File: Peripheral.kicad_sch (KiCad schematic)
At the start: 18 parts, among them J10 Conn_01x03, J11 Conn_01x03, J12 Conn_01x03, J2 Conn_01x04, J3 Conn_01x06, J4 Conn_01x06, J5 Conn_01x06, J6 Conn_01x07, J9 Conn_01x03

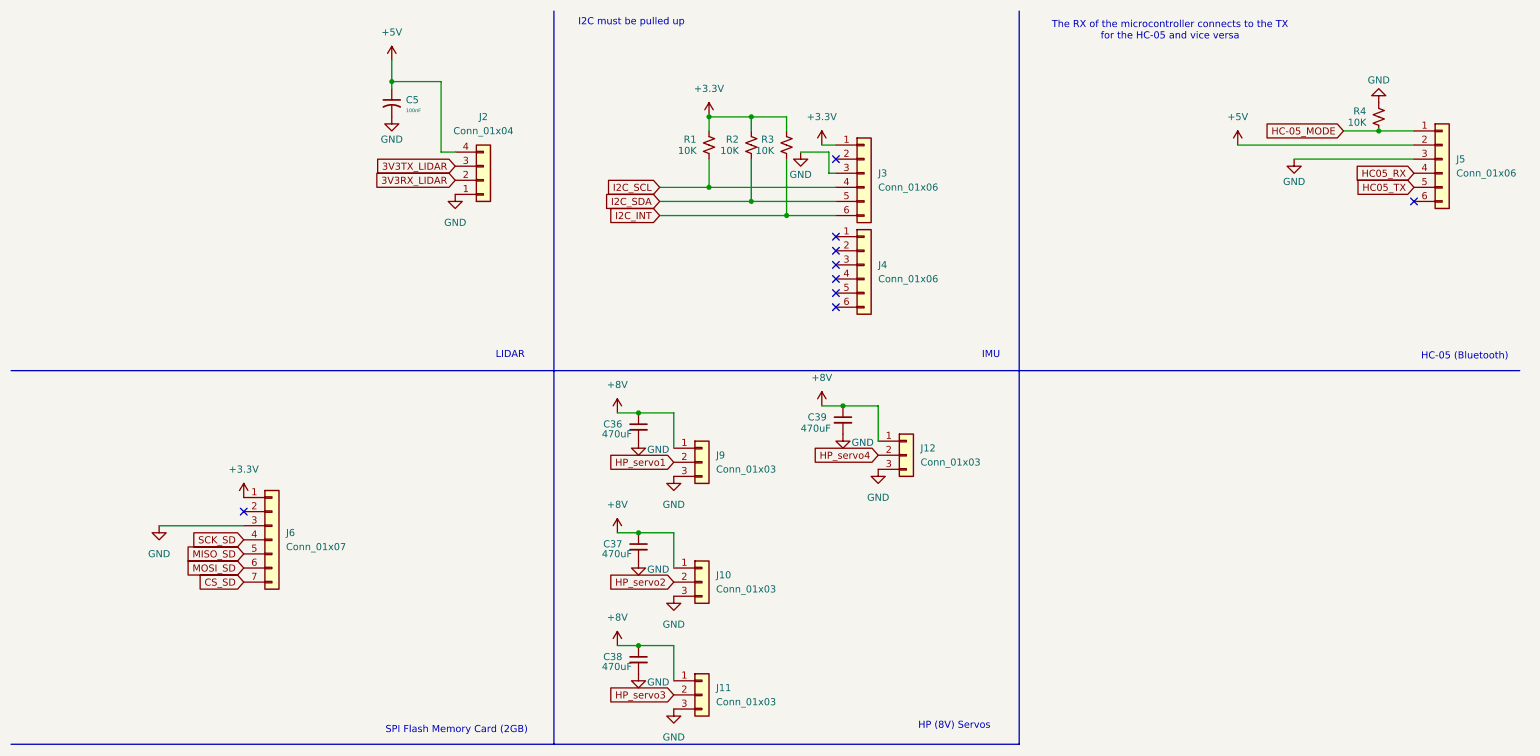
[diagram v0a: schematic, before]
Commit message: General Layout Complete
Completed general layout, beginning to add debugging components such as test points and
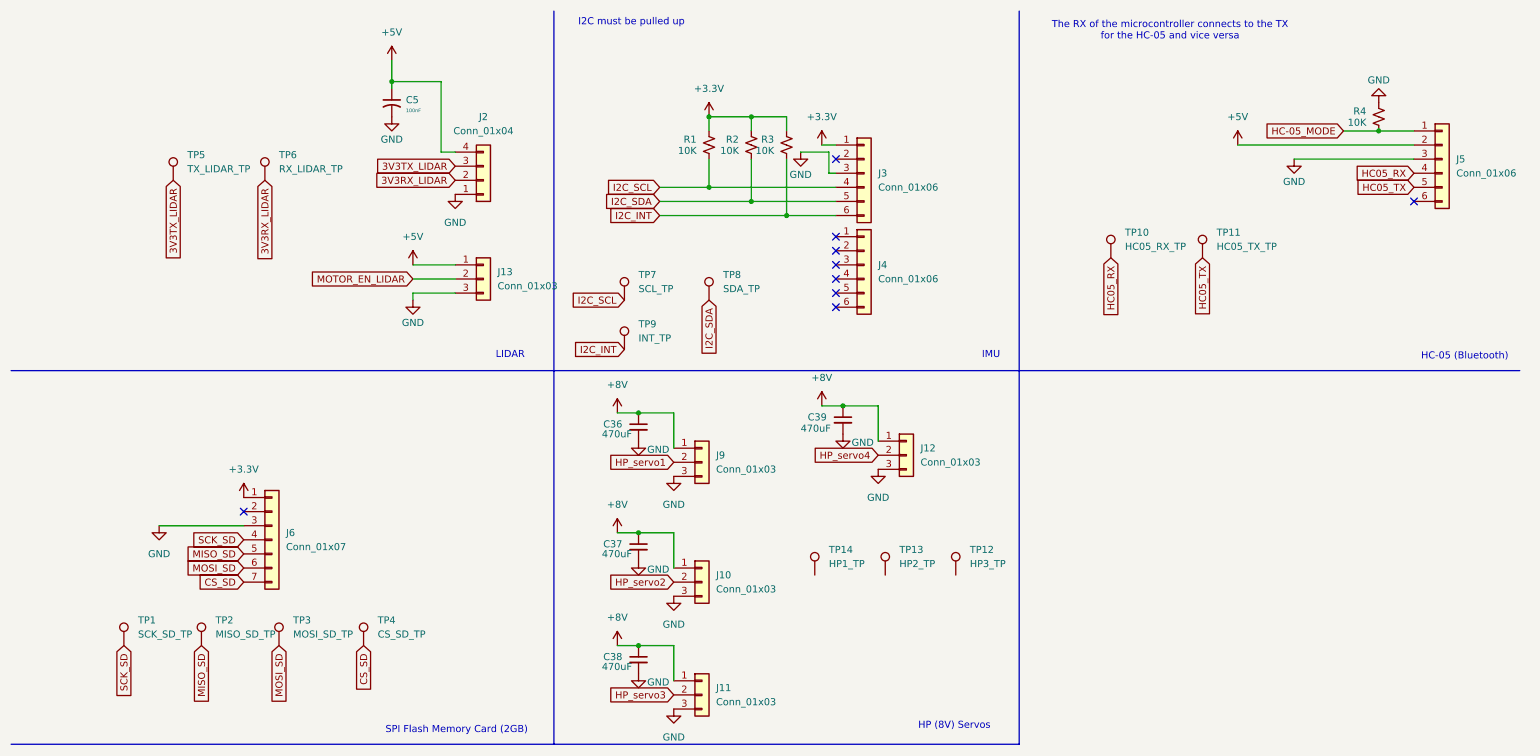
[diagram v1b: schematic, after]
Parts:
- added J13: Conn_01x03, Connector_PinHeader_2.54mm:PinHeader_1x03_P2.54mm_Vertical, symbol Connector_Generic:Conn_01x03
- added TP1: SCK_SD_TP, symbol Connector:TestPoint
- added TP10: HC05_RX_TP, symbol Connector:TestPoint
- added TP11: HC05_TX_TP, symbol Connector:TestPoint
- added TP12: HP3_TP, symbol Connector:TestPoint
- added TP13: HP2_TP, symbol Connector:TestPoint
- added TP14: HP1_TP, symbol Connector:TestPoint
- added TP2: MISO_SD_TP, symbol Connector:TestPoint
- added TP3: MOSI_SD_TP, symbol Connector:TestPoint
- added TP4: CS_SD_TP, symbol Connector:TestPoint
- added TP5: TX_LIDAR_TP, symbol Connector:TestPoint
- added TP6: RX_LIDAR_TP, symbol Connector:TestPoint
- added TP7: SCL_TP, symbol Connector:TestPoint
- added TP8: SDA_TP, symbol Connector:TestPoint
- added TP9: INT_TP, symbol Connector:TestPoint
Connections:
- net +5V: now also J13.1 (Pin_1)
- net 3V3RX_LIDAR: now also TP6.1
- net 3V3TX_LIDAR: now also TP5.1
- net CS_SD: now also TP4.1
- net GND: now also J13.3 (Pin_3)
- net HC05_RX: now also TP10.1
- net HC05_TX: now also TP11.1
- net I2C_INT: now also TP9.1
- net I2C_SCL: now also TP7.1
- net I2C_SDA: now also TP8.1
- net MISO_SD: now also TP2.1
- net MOSI_SD: now also TP3.1
- net SCK_SD: now also TP1.1
- new net MOTOR_EN_LIDAR: J13.2 (Pin_2)

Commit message: update
more work on testpoints
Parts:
- added TP15: HP4_TP, symbol Connector:TestPoint
- added TP16: GND_2, symbol Connector:TestPoint
- added TP17: GND_3, symbol Connector:TestPoint
- added TP18: GND_4, symbol Connector:TestPoint
- added TP19: GND_5, symbol Connector:TestPoint
- added TP20: GND_1, symbol Connector:TestPoint
- added TP21: GND_6, symbol Connector:TestPoint
- added TP22: GND_7, symbol Connector:TestPoint
- added TP23: GND_8, symbol Connector:TestPoint
- added TP24: GND_9, symbol Connector:TestPoint
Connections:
- net GND: now also TP16.1, TP17.1, TP18.1, TP19.1, TP20.1, TP21.1, TP22.1, TP23.1, TP24.1
- net HP_servo1: now also TP14.1
- net HP_servo2: now also TP13.1
- net HP_servo3: now also TP12.1
- net HP_servo4: now also TP15.1
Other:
- note added: "Test points for each motor"
- note added: "Test points for each peripheral"
- moved on the sheet: TP12, TP13

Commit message: testpoints on board
Organized testpoints on board. Still need to fix bus for general purpose GPIO and route traces for LEDs.
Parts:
- TP1, TP10, TP11, TP12, TP13, TP14, TP15, TP16, TP17, TP18, TP19, TP2, TP20, TP21, TP22, TP23, TP24, TP3, TP4, TP5, TP6, TP7, TP8, TP9: footprint (none) -> TestPoint:TestPoint_Keystone_5019_Miniature
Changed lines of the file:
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@@
 			)
 		)
-		(property "Footprint" ""
+		(property "Footprint" "TestPoint:TestPoint_Keystone_5019_Miniature"
 			(at 232.41 57.15 0)
 			(hide yes)
@@
 			)
 		)
-		(property "Footprint" ""
+		(property "Footprint" "TestPoint:TestPoint_Keystone_5019_Miniature"
 			(at 280.67 97.79 0)
 			(hide yes)
@@
 			)
 		)
-		(property "Footprint" ""
+		(property "Footprint" "TestPoint:TestPoint_Keystone_5019_Miniature"
 			(at 215.9 57.15 0)
 			(hide yes)
@@
 			)
 		)
-		(property "Footprint" ""
+		(property "Footprint" "TestPoint:TestPoint_Keystone_5019_Miniature"
 			(at 143.51 64.77 0)
 			(hide yes)
@@
 			)
 		)
-		(property "Footprint" ""
+		(property "Footprint" "TestPoint:TestPoint_Keystone_5019_Miniature"
 			(at 166.37 121.92 0)
 			(hide yes)
@@
 			)
 		)
-		(property "Footprint" ""
+		(property "Footprint" "TestPoint:TestPoint_Keystone_5019_Miniature"
 			(at 177.8 114.3 0)
 			(hide yes)
@@
 			)
 		)
-		(property "Footprint" ""
+		(property "Footprint" "TestPoint:TestPoint_Keystone_5019_Miniature"
 			(at 81.28 127 0)
 			(hide yes)
@@
 			)
 		)
-		(property "Footprint" ""
+		(property "Footprint" "TestPoint:TestPoint_Keystone_5019_Miniature"
 			(at 63.5 43.18 0)
 			(hide yes)
@@
 			)
 		)
-		(property "Footprint" ""
+		(property "Footprint" "TestPoint:TestPoint_Keystone_5019_Miniature"
 			(at 52.07 127 0)
 			(hide yes)
@@
 			)
 		)
-		(property "Footprint" ""
+		(property "Footprint" "TestPoint:TestPoint_Keystone_5019_Miniature"
 			(at 266.7 97.79 0)
 			(hide yes)
@@
 			)
 		)
-		(property "Footprint" ""
+		(property "Footprint" "TestPoint:TestPoint_Keystone_5019_Miniature"
 			(at 162.56 114.3 0)
 			(hide yes)
@@
 			)
 		)
-		(property "Footprint" ""
+		(property "Footprint" "TestPoint:TestPoint_Keystone_5019_Miniature"
 			(at 267.97 120.65 0)
 			(hide yes)
@@
 			)
 		)
-		(property "Footprint" ""
+		(property "Footprint" "TestPoint:TestPoint_Keystone_5019_Miniature"
 			(at 128.27 73.66 0)
 			(hide yes)
@@
 			)
 		)
-		(property "Footprint" ""
+		(property "Footprint" "TestPoint:TestPoint_Keystone_5019_Miniature"
 			(at 238.76 120.65 0)
 			(hide yes)
@@
 			)
 		)
-		(property "Footprint" ""
+		(property "Footprint" "TestPoint:TestPoint_Keystone_5019_Miniature"
 			(at 224.79 97.79 0)
 			(hide yes)
@@
 			)
 		)
-		(property "Footprint" ""
+		(property "Footprint" "TestPoint:TestPoint_Keystone_5019_Miniature"
 			(at 224.79 120.65 0)
 			(hide yes)
@@
 			)
 		)
-		(property "Footprint" ""
+		(property "Footprint" "TestPoint:TestPoint_Keystone_5019_Miniature"
 			(at 38.1 127 0)
 			(hide yes)
@@
 			)
 		)
-		(property "Footprint" ""
+		(property "Footprint" "TestPoint:TestPoint_Keystone_5019_Miniature"
 			(at 189.23 114.3 0)
 			(hide yes)
@@
 			)
 		)
-		(property "Footprint" ""
+		(property "Footprint" "TestPoint:TestPoint_Keystone_5019_Miniature"
 			(at 254 97.79 0)
 			(hide yes)
@@
 			)
 		)
-		(property "Footprint" ""
+		(property "Footprint" "TestPoint:TestPoint_Keystone_5019_Miniature"
 			(at 66.04 127 0)
 			(hide yes)
@@
 			)
 		)
-		(property "Footprint" ""
+		(property "Footprint" "TestPoint:TestPoint_Keystone_5019_Miniature"
 			(at 128.27 64.77 0)
 			(hide yes)
@@
 			)
 		)
-		(property "Footprint" ""
+		(property "Footprint" "TestPoint:TestPoint_Keystone_5019_Miniature"
 			(at 240.03 97.79 0)
 			(hide yes)
@@
 			)
 		)
-		(property "Footprint" ""
+		(property "Footprint" "TestPoint:TestPoint_Keystone_5019_Miniature"
 			(at 46.99 43.18 0)
 			(hide yes)
@@
 			)
 		)
-		(property "Footprint" ""
+		(property "Footprint" "TestPoint:TestPoint_Keystone_5019_Miniature"
 			(at 254 120.65 0)
 			(hide yes)

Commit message: almost completed board
need to clean up silkscreen, run thru checklist and verify, review datasheets
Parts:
- added R25, R26, R27, R28, R29, R30, R31, R32: 22, Resistor_SMD:R_0805_2012Metric_Pad1.20x1.40mm_HandSolder, symbol Device:R_Small_US
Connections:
- net 3V3RX_LIDAR: now also R26.1, R26.2
- net 3V3TX_LIDAR: now also R25.1, R25.2
- net CS_SD: now also R29.1, R29.2
- net HC05_RX: now also R27.1, R27.2
- net HC05_TX: now also R28.1, R28.2
- net MISO_SD: now also R31.1, R31.2
- net MOSI_SD: now also R30.1, R30.2
- net SCK_SD: now also R32.1, R32.2
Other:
- moved on the sheet: TP5, TP6

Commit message: completed v1 board with outputs
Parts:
- added TP25: state hc05, TestPoint:TestPoint_Keystone_5019_Miniature, symbol Connector:TestPoint
- R1, R2, R3: value 10K -> 4.7K
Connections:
- net at J5.6 (Pin_6): now also TP25.1
- no-connect marks 9 -> 8
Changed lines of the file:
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@@
 		(at 54.61 102.87)
 	)
-	(no_connect
-		(at 265.43 46.99)
-	)
 	(wire
 		(pts
@@
 	(wire
 		(pts
+			(xy 265.43 55.88) (xy 250.19 55.88)
+		)
+		(stroke
+			(width 0)
+			(type default)
+		)
+	)
+	(wire
+		(pts
 			(xy 248.92 101.6) (xy 248.92 105.41)
 		)
@@
 	(wire
 		(pts
+			(xy 265.43 46.99) (xy 265.43 55.88)
+		)
+		(stroke
+			(width 0)
+			(type default)
+		)
+	)
+	(wire
+		(pts
 			(xy 219.71 120.65) (xy 219.71 124.46)
 		)
@@
 			)
 		)
-		(property "Value" "10K"
+		(property "Value" "4.7K"
 			(at 140.462 37.846 0)
 			(show_name no)
@@
 			)
 		)
-		(property "Value" "10K"
+		(property "Value" "4.7K"
 			(at 132.842 37.846 0)
 			(show_name no)
@@
 	)
 	(symbol
+		(lib_id "Connector:TestPoint")
+		(at 250.19 55.88 0)
+		(unit 1)
+		(body_style 1)
+		(exclude_from_sim no)
+		(in_bom yes)
+		(on_board yes)
+		(in_pos_files yes)
+		(dnp no)
+		(fields_autoplaced yes)
+		(property "Reference" "TP25"
+			(at 252.73 51.3079 0)
+			(show_name no)
+			(do_not_autoplace no)
+			(effects
+				(font
+					(size 1.27 1.27)
+				)
+				(justify left)
+			)
+		)
+		(property "Value" "state hc05"
+			(at 252.73 53.8479 0)
+			(show_name no)
+			(do_not_autoplace no)
+			(effects
+				(font
+					(size 1.27 1.27)
+				)
+				(justify left)
+			)
+		)
+		(property "Footprint" "TestPoint:TestPoint_Keystone_5019_Miniature"
+			(at 255.27 55.88 0)
+			(hide yes)
+			(show_name no)
+			(do_not_autoplace no)
+			(effects
+				(font
+					(size 1.27 1.27)
+				)
+			)
+		)
+		(property "Datasheet" ""
+			(at 255.27 55.88 0)
+			(hide yes)
+			(show_name no)
+			(do_not_autoplace no)
+			(effects
+				(font
+					(size 1.27 1.27)
+				)
+			)
+		)
+		(property "Description" "test point"
+			(at 250.19 55.88 0)
+			(hide yes)
+			(show_name no)
+			(do_not_autoplace no)
+			(effects
+				(font
+					(size 1.27 1.27)
+				)
+			)
+		)
+		(pin "1"
+		)
+		(instances
+			(project "Bellbot"
+				(path "/e8e381ed-df8a-48a3-822a-37f3233d3329/8c8120b7-7eca-4130-99a8-268717bfff76"
+					(reference "TP25")
+					(unit 1)
+				)
+			)
+		)
+	)
+	(symbol
 		(lib_id "Device:R_Small_US")
 		(at 259.08 31.75 0)
@@
 			)
 		)
-		(property "Value" "10K"
+		(property "Value" "4.7K"
 			(at 146.812 37.846 0)
 			(show_name no)
